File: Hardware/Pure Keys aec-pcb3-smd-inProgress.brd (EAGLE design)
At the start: 99 x 98.7 mm, 71 parts, among them Q2 20MHz, T1 2N3904, U1 ATMEGA328P_TQFP, U2 LM4040

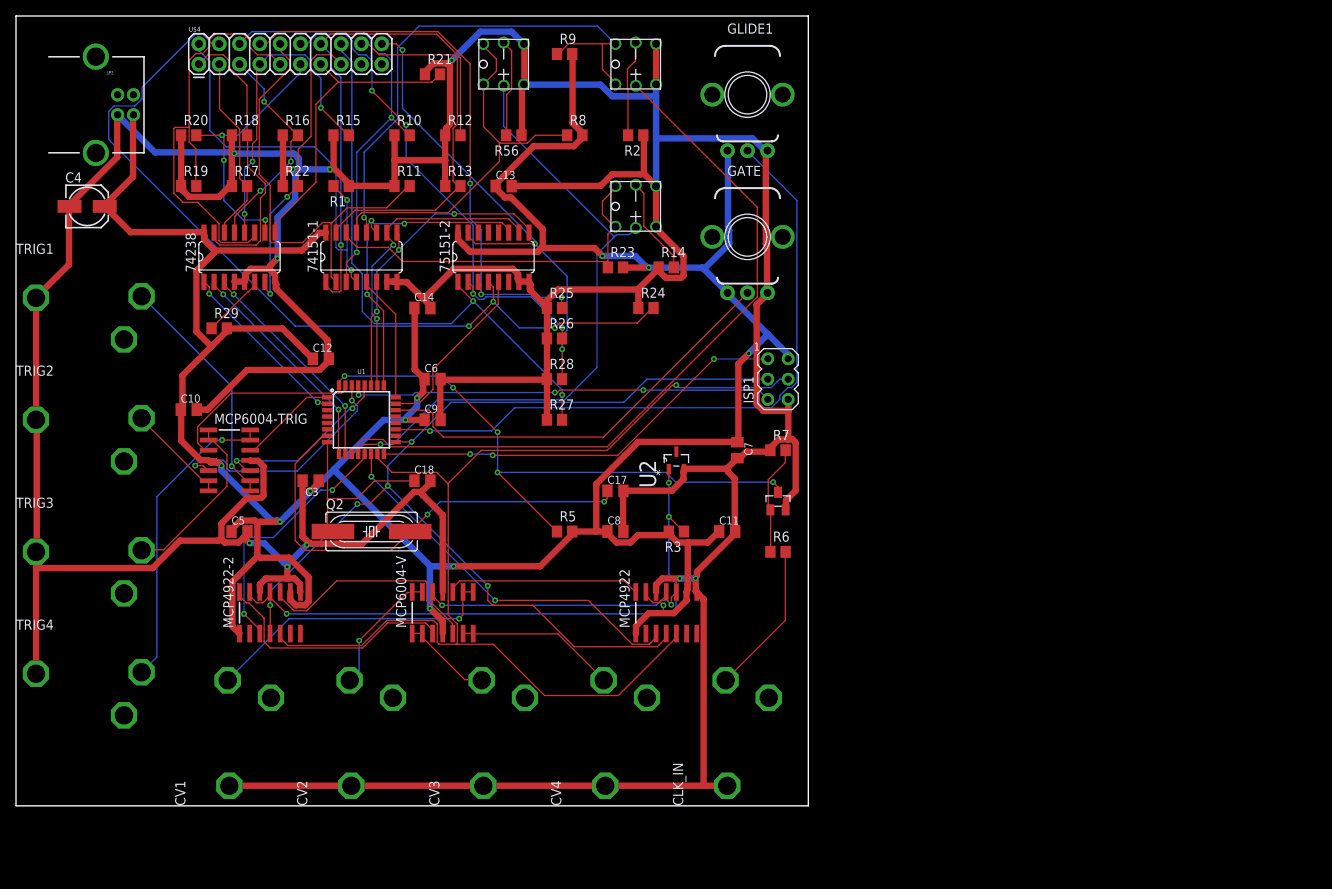
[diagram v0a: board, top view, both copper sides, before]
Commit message: changed cs select
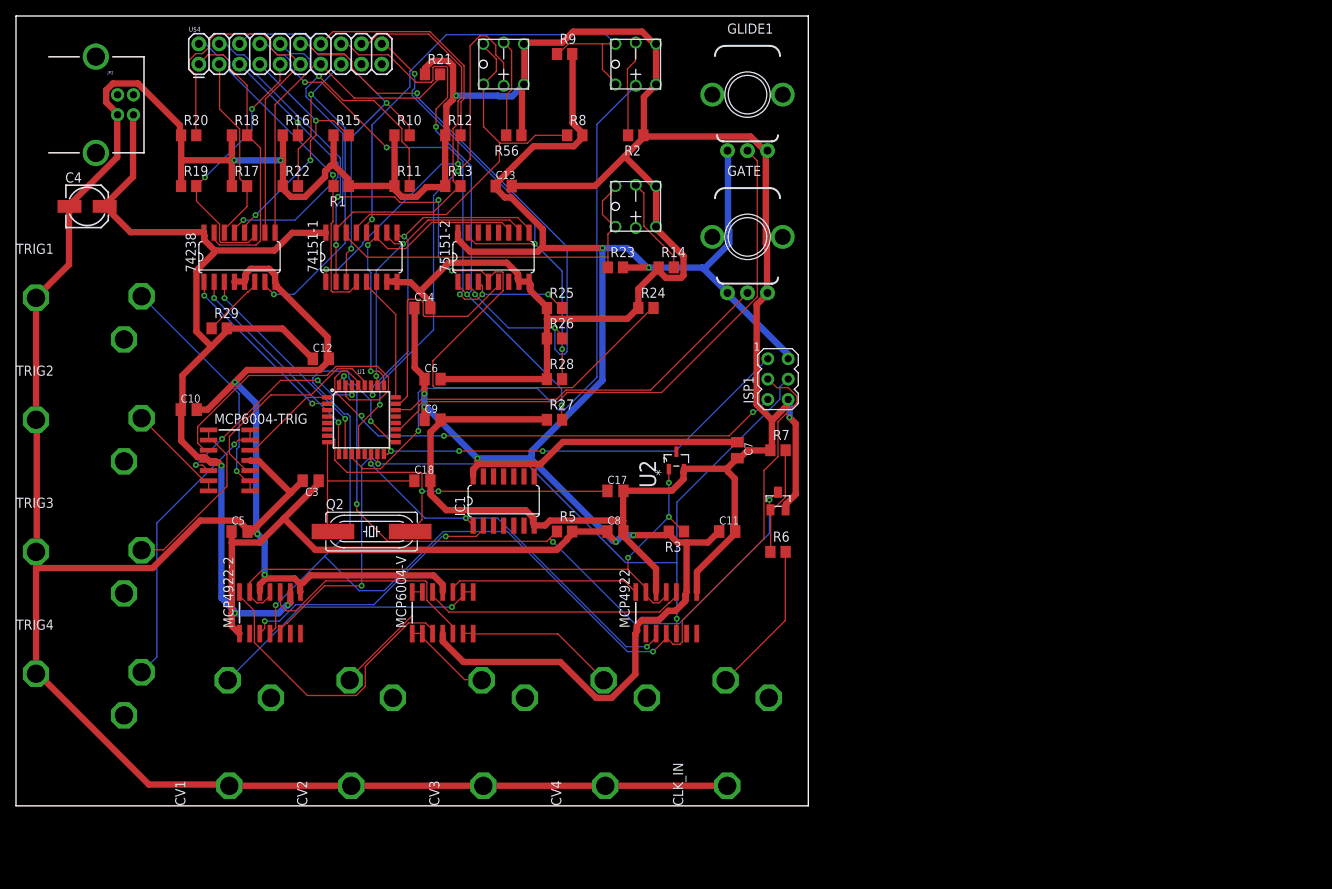
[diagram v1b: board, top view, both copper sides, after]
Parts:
- added IC1: 74AC04D, 74xx-eu:SO14
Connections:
- new net BUTLED3: BUT3.A
- net 5V: now also IC1.14
- net BUTLED1: no longer BUT3.A
- net CS1: now also IC1.1
- net CS2: now also IC1.2; no longer U1.13
- net GND: now also IC1.7
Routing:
- net 5V: track 407.8 -> 473.4 mm
- net GND: track 718.6 -> 746.9 mm, vias 10 -> 7
- net MOSI: track 139.9 -> 112.0 mm, vias 1 -> 3
- net SCK: track 127.2 -> 153.7 mm, vias 5 -> 3
- net T4: track 56.1 -> 32.9 mm, vias 0 -> 2
- net T5: track 33.4 -> 50.5 mm, vias 3 -> 0
- net TRIG3: track 24.7 -> 40.4 mm
- net BR2: track 61.9 -> 77.6 mm, vias 4 -> 3
- net T7: track 37.6 -> 51.5 mm
- net POT1: track 84.5 -> 71.2 mm, vias 1 -> 0
- net BUTLED1: track 79.6 -> 66.6 mm, vias 1 -> 2
- net CLK_IN: track 75.5 -> 88.2 mm, vias 5 -> 4
- net BUTLED2: track 92.5 -> 79.9 mm, vias 0 -> 1
- net N$10: track 58.2 -> 46.4 mm
- net RST: track 53.1 -> 64.5 mm
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
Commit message: New Board Shape and layout
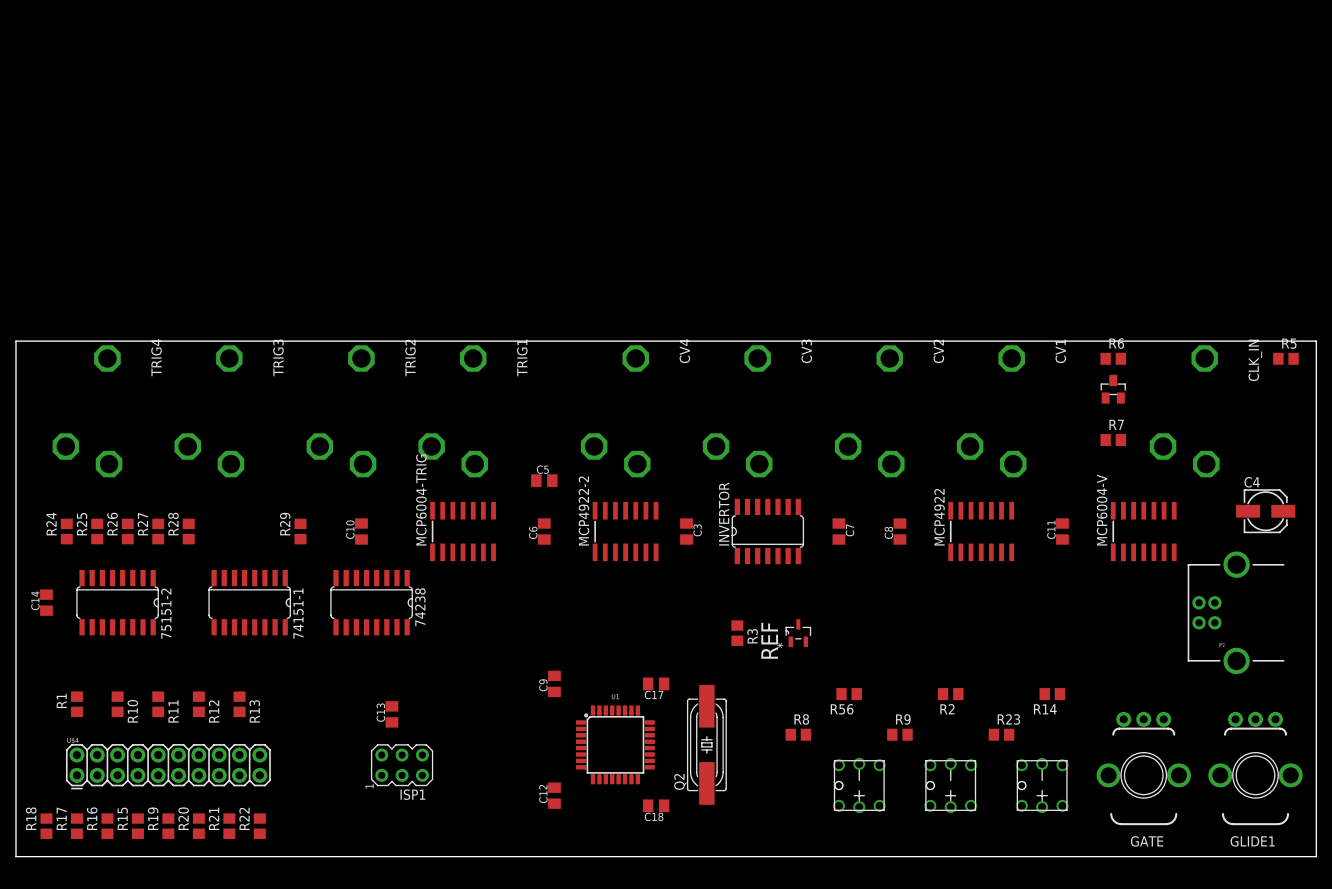
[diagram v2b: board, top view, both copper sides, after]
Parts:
- removed IC1: 74AC04D, 74xx-eu:SO14
- removed T1: 2N3904, INSTRUO:TRANSISTOR_SINGLE_N-TYPE
- removed U2: LM4040, GMSN-R2Project:SOT95P237X112-3N
- added CLOCK: 2N3904, INSTRUO:TRANSISTOR_SINGLE_N-TYPE
- added INVERTOR: 74AC04D, 74xx-eu:SO14
- added REF: LM4040, GMSN-R2Project:SOT95P237X112-3N
- moved C4 152.2 mm to (156.2, 36.8)
- moved JP2 151.1 mm to (149.9, 24.1), turned to 180 degrees
- moved CV1 113.9 mm to (124.5, 58.4), turned to 270 degrees
- moved GLIDE1 106.2 mm to (154.9, 3.81), turned to 180 degrees
- moved BUT1 100.5 mm to (105.4, 2.54)
- moved BUT2 98.4 mm to (116.8, 2.54)
- moved R21 97.4 mm to (26.7, -2.54), turned to 90 degrees
- moved R9 94.9 mm to (110.5, 8.89)
- moved R5 92.7 mm to (158.8, 55.9)
- moved U$4 90.2 mm to (7.62, 3.81)
- moved R15 90.0 mm to (15.2, -2.54), turned to 90 degrees
- moved R18 89.7 mm to (3.81, -2.54), turned to 90 degrees
- moved R16 89.3 mm to (11.4, -2.54), turned to 90 degrees
- moved CV2 89.1 mm to (109.2, 58.4), turned to 270 degrees
- moved BUT3 88.4 mm to (128.3, 2.54)
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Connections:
- net 3VREF: now also REF.1; no longer U2.1
- net 5V: now also INVERTOR.14; no longer IC1.14
- net BUTLED3: now also U1.13
- net CLK_IN: now also CLOCK.C; no longer T1.C
- net CS1: now also INVERTOR.1; no longer IC1.1
- net CS2: now also INVERTOR.2; no longer IC1.2
- net GND: now also CLOCK.E, INVERTOR.7, REF.2; no longer IC1.7, T1.E, U2.2
- net N$17: now also CLOCK.B; no longer T1.B
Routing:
- net GND: track 746.9 -> 0.00 mm, vias 7 -> 0
- net 5V: track 473.4 -> 0.00 mm, vias 10 -> 0
- net SCK: track 153.7 -> 0.00 mm, vias 3 -> 0
- net MOSI: track 112.0 -> 0.00 mm, vias 3 -> 0
- net BR0: track 106.7 -> 0.00 mm, vias 3 -> 0
- net CLK_IN: track 88.2 -> 0.00 mm, vias 4 -> 0
- net BUTLED2: track 79.9 -> 0.00 mm, vias 1 -> 0
- net 3VREF: track 78.6 -> 0.00 mm, vias 3 -> 0
- net BR2: track 77.6 -> 0.00 mm, vias 3 -> 0
- net POT1: track 71.2 -> 0.00 mm
- net BR3: track 70.8 -> 0.00 mm, vias 3 -> 0
- net BUTLED1: track 66.6 -> 0.00 mm, vias 2 -> 0
- net RST: track 64.5 -> 0.00 mm, vias 3 -> 0
- net BR1: track 64.5 -> 0.00 mm, vias 5 -> 0
- net BUT2: track 64.1 -> 0.00 mm, vias 1 -> 0
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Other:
- board size 99 x 98.7 mm -> 162.5 x 64.4 mm

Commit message: New Board Shape and layout
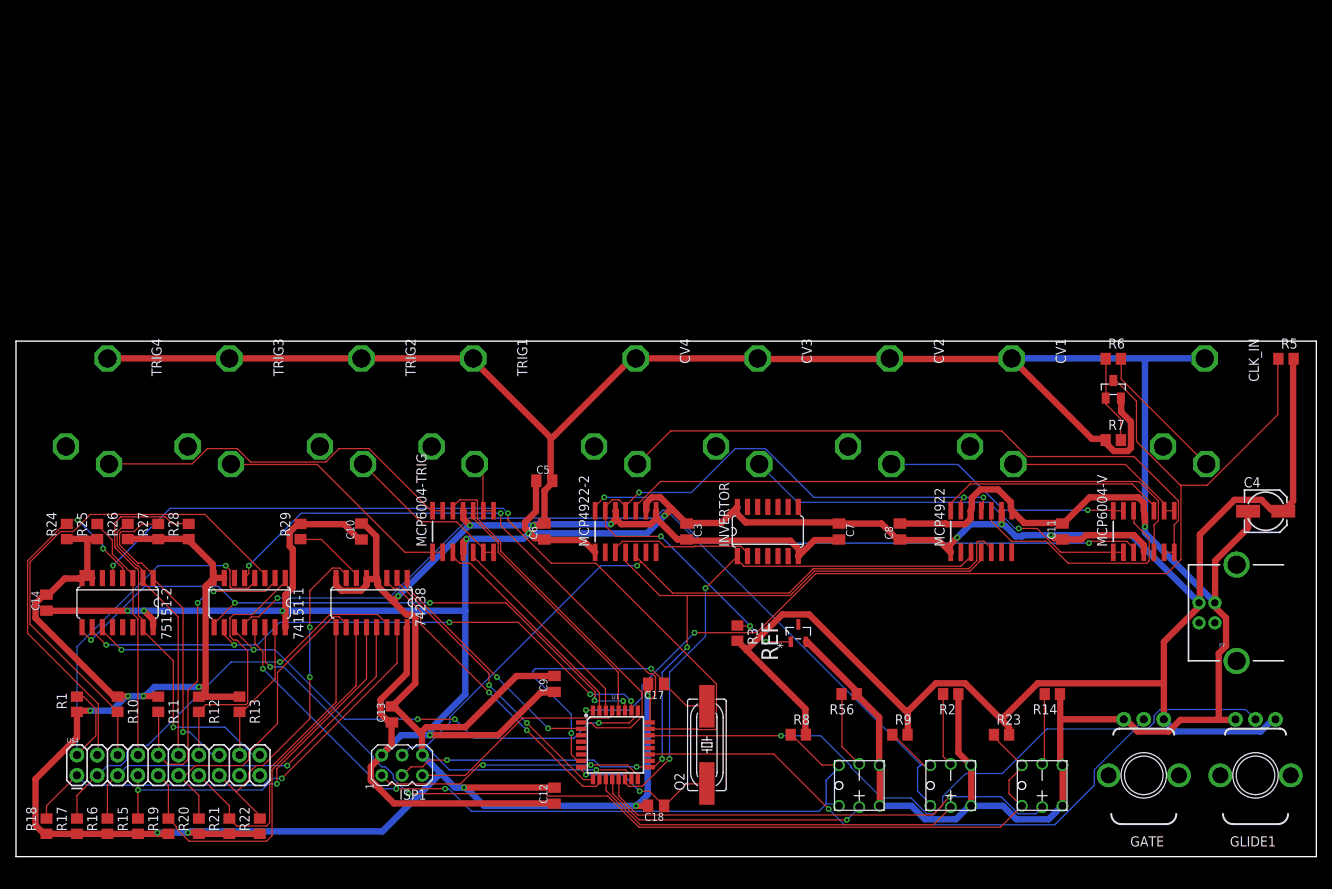
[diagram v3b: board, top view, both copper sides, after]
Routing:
- net GND: track 0.00 -> 749.5 mm, vias 0 -> 14
- net 5V: track 0.00 -> 475.9 mm, vias 0 -> 10
- net CLK_IN: track 0.00 -> 132.9 mm, vias 0 -> 2
- net BUT3: track 0.00 -> 120.7 mm, vias 0 -> 2
- net MOSI: track 0.00 -> 119.7 mm, vias 0 -> 2
- net BUT2: track 0.00 -> 117.6 mm, vias 0 -> 1
- net SCK: track 0.00 -> 106.0 mm, vias 0 -> 4
- net DBIN: track 0.00 -> 103.6 mm, vias 0 -> 2
- net BUT1: track 0.00 -> 98.6 mm, vias 0 -> 3
- net 3VREF: track 0.00 -> 91.5 mm, vias 0 -> 6
- net POT1: track 0.00 -> 87.5 mm, vias 0 -> 1
- net A2IN: track 0.00 -> 83.5 mm, vias 0 -> 5
- net N$25: track 0.00 -> 80.9 mm
- net A0IN: track 0.00 -> 78.5 mm, vias 0 -> 5
- net A1IN: track 0.00 -> 77.7 mm, vias 0 -> 5
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
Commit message: THinner board
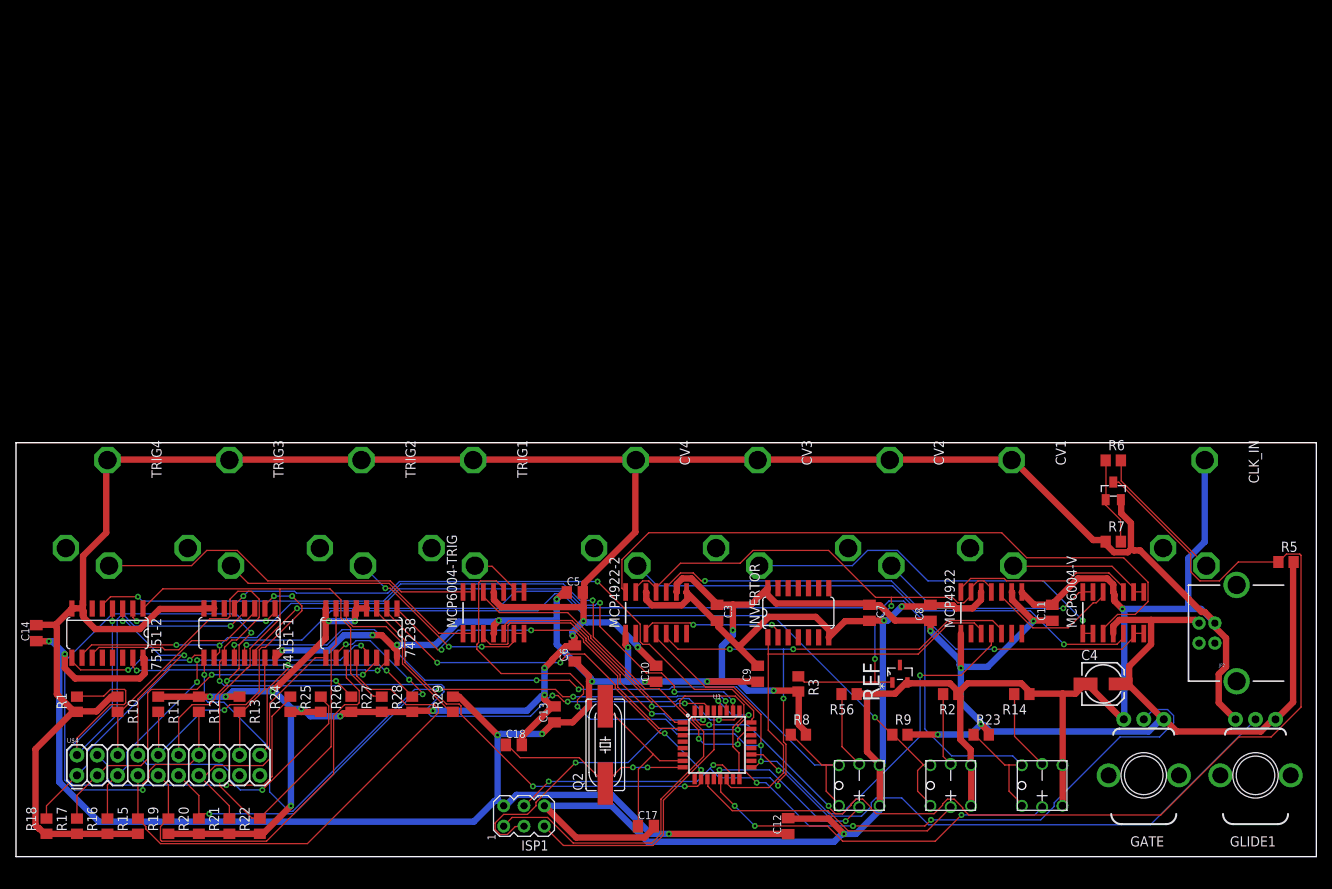
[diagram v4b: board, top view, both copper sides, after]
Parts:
- moved C10 40.9 mm to (80.0, 16.5)
- moved R25 35.3 mm to (38.1, 12.7)
- moved R28 35.3 mm to (49.5, 12.7)
- moved R24 35.3 mm to (34.3, 12.7)
- moved R26 35.3 mm to (41.9, 12.7)
- moved R27 35.3 mm to (45.7, 12.7)
- moved C4 29.6 mm to (135.9, 15.2)
- moved C12 29.5 mm to (96.5, -2.54)
- moved R29 28.8 mm to (54.6, 12.7)
- moved C9 25.4 mm to (92.7, 16.5)
- moved R5 25.4 mm to (158.8, 30.5)
- moved C13 20.3 mm to (67.3, 11.4)
- moved C18 19.3 mm to (62.2, 7.62), turned to 0 degrees
- moved C17 17.8 mm to (78.7, -2.54), turned to 0 degrees
- moved ISP1 16.5 mm to (63.5, -1.27)
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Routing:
- net MK3: track 33.0 -> 70.3 mm, vias 0 -> 2
- net MK1: track 64.1 -> 28.2 mm
- net A0IN: track 78.5 -> 114.3 mm, vias 5 -> 4
- net BR1: track 31.0 -> 59.5 mm, vias 0 -> 3
- net TRIG1: track 32.5 -> 60.0 mm, vias 0 -> 4
- net MISO: track 34.4 -> 60.9 mm, vias 2 -> 0
- net BR3: track 39.4 -> 65.1 mm, vias 1 -> 0
- net GND: track 749.5 -> 725.4 mm, vias 14 -> 18
- net A2IN: track 83.5 -> 105.9 mm, vias 5 -> 6
- net BR2: track 32.9 -> 53.4 mm, vias 0 -> 4
- net 5V: track 475.9 -> 455.4 mm, vias 10 -> 21
- net BR0: track 46.0 -> 65.1 mm
- net A1IN: track 77.7 -> 96.6 mm
- net T3: track 47.3 -> 65.9 mm, vias 2 -> 0
- net MOSI: track 119.7 -> 101.7 mm, vias 2 -> 6
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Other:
- board size 162.5 x 64.4 mm -> 162.5 x 51.7 mm

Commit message: reroutes
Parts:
- moved ISP1 87.6 mm to (151.1, 0.00), turned to 180 degrees
- moved BUT2 67.3 mm to (49.5, 1.27)
- moved BUT3 67.3 mm to (61.0, 1.27)
- moved BUT1 66.1 mm to (39.4, 1.27)
- moved R14 63.8 mm to (62.2, 7.62)
- moved GATE 62.3 mm to (78.7, 1.27)
- moved R2 61.3 mm to (55.9, 7.62)
- moved R56 61.3 mm to (43.2, 7.62)
- moved GLIDE1 61.0 mm to (94.0, 1.27)
- moved R8 61.0 mm to (36.8, 7.62)
- moved R9 61.0 mm to (49.5, 7.62)
- moved R23 52.1 mm to (68.6, 7.62)
- moved C18 46.8 mm to (108.0, -2.54), turned to 180 degrees
- moved C9 43.6 mm to (135.9, 10.2), turned to 270 degrees
- moved Q2 40.8 mm to (114.3, 3.81)
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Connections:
- net 5V: now also U1.6
- net GND: now also 75151-2.12, 75151-2.13, 75151-2.14, U1.21
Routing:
- net CLK_IN: track 141.2 -> 47.7 mm
- net GND: track 725.4 -> 642.3 mm, vias 18 -> 8
- net BUTLED1: track 22.3 -> 88.1 mm, vias 2 -> 1
- net BUT1: track 97.2 -> 32.9 mm, vias 3 -> 0
- net BUT3: track 130.8 -> 69.4 mm
- net A1OUT: track 50.8 -> 109.8 mm
- net TRIG2: track 32.4 -> 91.4 mm
- net DAIN: track 76.3 -> 135.2 mm, vias 2 -> 4
- net TRIG3: track 37.7 -> 94.9 mm
- net MK3: track 70.3 -> 13.3 mm, vias 2 -> 0
- net A2OUT: track 52.9 -> 97.4 mm, vias 2 -> 4
- net BUTLED2: track 34.8 -> 78.9 mm, vias 0 -> 1
- net A0OUT: track 45.2 -> 88.4 mm
- net T4: track 51.7 -> 92.7 mm, vias 0 -> 2
- net 5V: track 455.4 -> 414.7 mm, vias 21 -> 11
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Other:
- board size 162.5 x 51.7 mm -> 158.7 x 51.7 mm
